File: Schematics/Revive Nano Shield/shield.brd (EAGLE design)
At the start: 35.6 x 63.5 mm, 24 parts

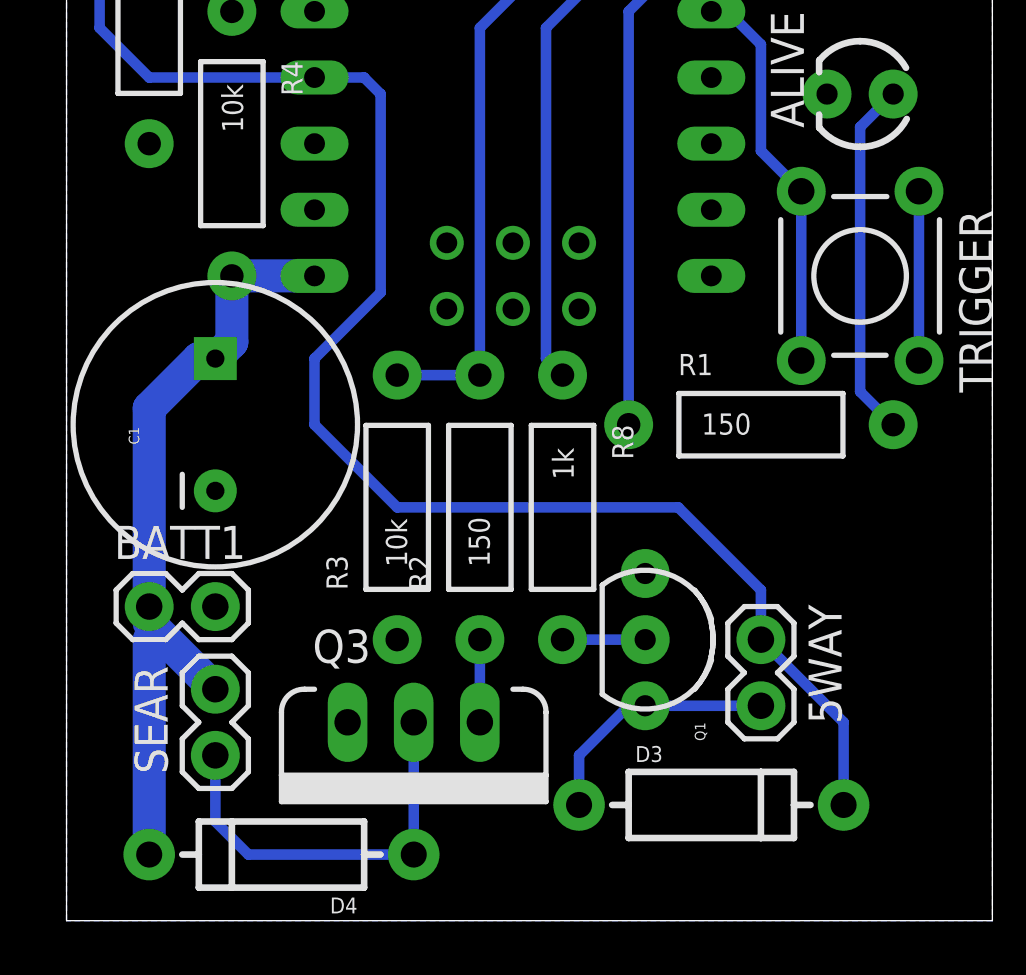
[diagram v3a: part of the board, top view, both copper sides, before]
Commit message: Moved around connectors to make them more accessible
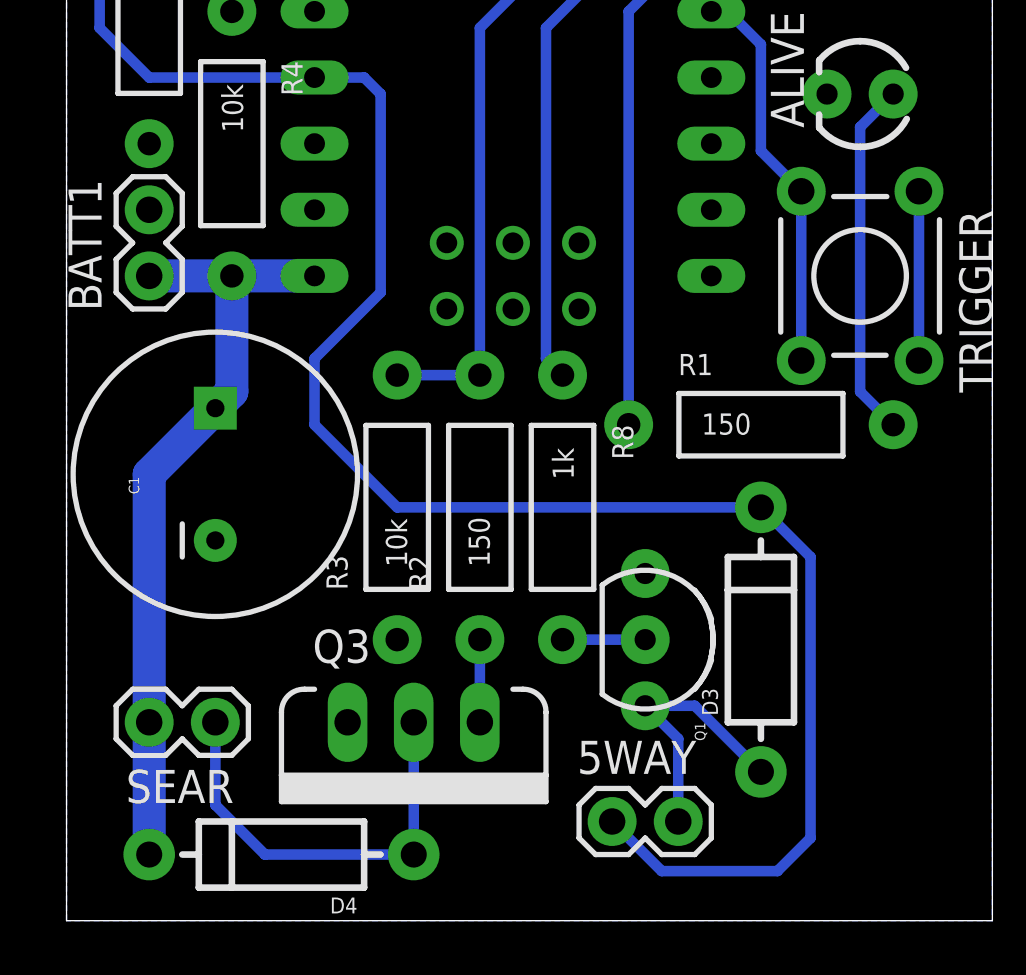
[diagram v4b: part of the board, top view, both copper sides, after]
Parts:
- moved BATT1 12.7 mm to (3.17, 24.8), turned to 90 degrees
- moved 5WAY 9.03 mm to (21.0, 3.81), turned to 0 degrees
- moved D3 6.63 mm to (26.7, 10.8), turned to 90 degrees
- moved SEAR 2.84 mm to (3.17, 7.62), turned to 0 degrees
- moved C1 1.91 mm to (5.71, 17.1)
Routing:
- net 5V: track 72.0 -> 83.5 mm
- net 9V: track 31.3 -> 29.9 mm
- net N$7: track 15.8 -> 16.7 mm
- net N$15: track 9.68 -> 10.5 mm
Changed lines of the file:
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@@
 </autorouter>
 <elements>
-<element name="5WAY" library="SparkFun" package="1X02" value="" x="26.67" y="10.795" rot="R270"/>
+<element name="5WAY" library="SparkFun" package="1X02" value="" x="20.955" y="3.81"/>
 <element name="ALIVE" library="SparkFun" package="LED3MM" value="" x="30.48" y="31.75" smashed="yes" rot="R180">
 <attribute name="NAME" x="27.051" y="34.925" size="1.27" layer="25" ratio="10" rot="R270"/>
 <attribute name="VALUE" x="28.575" y="33.401" size="1.27" layer="27" ratio="10" rot="R180"/>
 </element>
-<element name="BATT1" library="SparkFun" package="1X02" value="" x="3.175" y="12.065"/>
-<element name="C1" library="SparkFun" package="CPOL-RADIAL-1000UF-25V" value="2200uF" x="5.715" y="19.05" rot="R90"/>
-<element name="D3" library="SparkFun" package="DIODE-1N4001" value="" x="24.765" y="4.445"/>
+<element name="BATT1" library="SparkFun" package="1X02" value="" x="3.175" y="24.765" rot="R90"/>
+<element name="C1" library="SparkFun" package="CPOL-RADIAL-1000UF-25V" value="2200uF" x="5.715" y="17.145" rot="R90"/>
+<element name="D3" library="SparkFun" package="DIODE-1N4001" value="" x="26.67" y="10.795" rot="R90"/>
 <element name="D4" library="SparkFun" package="DIODE-1N4001" value="" x="8.255" y="2.54" rot="R180"/>
 <element name="DOWN" library="SparkFun" package="TACTILE-PTH" value="" x="30.48" y="57.785" rot="R270"/>
@@
 <element name="R6" library="SparkFun" package="AXIAL-0.4" value="1M" x="6.35" y="43.18" rot="R90"/>
 <element name="R8" library="SparkFun" package="AXIAL-0.4" value="1k" x="19.05" y="15.875" rot="R270"/>
-<element name="SEAR" library="SparkFun" package="1X02" value="" x="5.715" y="8.89" smashed="yes" rot="R270">
-<attribute name="NAME" x="3.8862" y="5.6388" size="1.27" layer="25" ratio="10" rot="R90"/>
-<attribute name="VALUE" x="2.54" y="10.16" size="1.27" layer="27" rot="R270"/>
+<element name="SEAR" library="SparkFun" package="1X02" value="" x="3.175" y="7.62" smashed="yes">
+<attribute name="NAME" x="6.4262" y="5.7912" size="1.27" layer="25" ratio="10" rot="R180"/>
+<attribute name="VALUE" x="1.905" y="4.445" size="1.27" layer="27"/>
 </element>
 <element name="SEL" library="SparkFun" package="TACTILE-PTH" value="" x="30.48" y="48.895" rot="R270"/>
@@
 <contactref element="C1" pad="1"/>
 <contactref element="R4" pad="P$2"/>
-<wire x1="3.175" y1="12.065" x2="3.175" y2="11.43" width="0.4064" layer="16"/>
-<wire x1="3.175" y1="11.43" x2="3.175" y2="10.795" width="0.4064" layer="16"/>
-<wire x1="3.175" y1="10.795" x2="3.81" y2="10.795" width="0.4064" layer="16"/>
 <wire x1="9.525" y1="24.765" x2="6.35" y2="24.765" width="1.27" layer="16"/>
-<wire x1="6.35" y1="24.765" x2="6.35" y2="22.225" width="1.27" layer="16"/>
-<wire x1="6.35" y1="22.225" x2="5.715" y2="21.59" width="1.27" layer="16"/>
-<wire x1="5.715" y1="21.59" x2="5.08" y2="21.59" width="1.27" layer="16"/>
-<wire x1="5.08" y1="21.59" x2="3.175" y2="19.685" width="1.27" layer="16"/>
-<wire x1="3.175" y1="19.685" x2="3.175" y2="12.065" width="1.27" layer="16"/>
-<wire x1="3.175" y1="10.795" x2="3.175" y2="2.54" width="1.27" layer="16"/>
-<wire x1="5.715" y1="8.89" x2="3.175" y2="11.43" width="1.27" layer="16"/>
+<wire x1="3.175" y1="24.765" x2="6.35" y2="24.765" width="1.27" layer="16"/>
+<wire x1="6.35" y1="24.765" x2="6.35" y2="20.32" width="1.27" layer="16"/>
+<wire x1="6.35" y1="20.32" x2="5.715" y2="19.685" width="1.27" layer="16"/>
+<wire x1="5.715" y1="19.685" x2="3.175" y2="17.145" width="1.27" layer="16"/>
+<wire x1="3.175" y1="17.145" x2="3.175" y2="7.62" width="1.27" layer="16"/>
+<wire x1="3.175" y1="7.62" x2="3.175" y2="2.54" width="1.27" layer="16"/>
 </signal>
 <signal name="GND">
@@
 <contactref element="D3" pad="C"/>
 <contactref element="5WAY" pad="1"/>
-<wire x1="29.845" y1="4.445" x2="29.845" y2="7.62" width="0.4064" layer="16"/>
-<wire x1="29.845" y1="7.62" x2="26.67" y2="10.795" width="0.4064" layer="16"/>
-<wire x1="26.67" y1="10.795" x2="26.67" y2="12.7" width="0.4064" layer="16"/>
-<wire x1="26.67" y1="12.7" x2="23.495" y2="15.875" width="0.4064" layer="16"/>
-<wire x1="23.495" y1="15.875" x2="12.7" y2="15.875" width="0.4064" layer="16"/>
+<wire x1="26.67" y1="15.875" x2="12.7" y2="15.875" width="0.4064" layer="16"/>
+<wire x1="20.955" y1="3.81" x2="22.86" y2="1.905" width="0.4064" layer="16"/>
+<wire x1="22.86" y1="1.905" x2="27.305" y2="1.905" width="0.4064" layer="16"/>
+<wire x1="27.305" y1="1.905" x2="28.575" y2="3.175" width="0.4064" layer="16"/>
+<wire x1="28.575" y1="3.175" x2="28.575" y2="13.97" width="0.4064" layer="16"/>
+<wire x1="28.575" y1="13.97" x2="26.67" y2="15.875" width="0.4064" layer="16"/>
 </signal>
 <signal name="TRIGGER">
@@
 <contactref element="D3" pad="A"/>
 <contactref element="5WAY" pad="2"/>
-<wire x1="26.67" y1="8.255" x2="22.225" y2="8.255" width="0.4064" layer="16"/>
-<wire x1="22.225" y1="8.255" x2="21.59" y2="8.255" width="0.4064" layer="16"/>
-<wire x1="21.59" y1="8.255" x2="19.685" y2="6.35" width="0.4064" layer="16"/>
-<wire x1="19.685" y1="6.35" x2="19.685" y2="4.445" width="0.4064" layer="16"/>
+<wire x1="22.225" y1="8.255" x2="24.13" y2="8.255" width="0.4064" layer="16"/>
+<wire x1="24.13" y1="8.255" x2="26.67" y2="5.715" width="0.4064" layer="16"/>
+<wire x1="23.495" y1="3.81" x2="23.495" y2="6.985" width="0.4064" layer="16"/>
+<wire x1="23.495" y1="6.985" x2="22.225" y2="8.255" width="0.4064" layer="16"/>
 </signal>
 <signal name="UP_BTN">
@@
 <contactref element="Q3" pad="2"/>
 <contactref element="SEAR" pad="2"/>
-<wire x1="13.335" y1="2.54" x2="6.985" y2="2.54" width="0.4064" layer="16"/>
 <wire x1="13.335" y1="2.54" x2="13.335" y2="7.62" width="0.4064" layer="16"/>
-<wire x1="5.715" y1="6.35" x2="5.715" y2="3.81" width="0.4064" layer="16"/>
-<wire x1="5.715" y1="3.81" x2="6.985" y2="2.54" width="0.4064" layer="16"/>
+<wire x1="5.715" y1="7.62" x2="5.715" y2="4.445" width="0.4064" layer="16"/>
+<wire x1="5.715" y1="4.445" x2="7.62" y2="2.54" width="0.4064" layer="16"/>
+<wire x1="7.62" y1="2.54" x2="13.335" y2="2.54" width="0.4064" layer="16"/>
 </signal>
 <signal name="N$1">

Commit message: Updated schematics
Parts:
- removed SENSOR: (no value), SparkFun:1X04
- added A/C_EYE: (no value), SparkFun:1X04
- added SLG_EYE: (no value), SparkFun-Connectors:1X03
- added SPI: (no value), SparkFun-Connectors:1X07
- R4, R5, R6, R9: device SparkFun:AXIAL-0.4 -> resistor:0309V
- moved R6 20.4 mm to (4.45, 63.5), turned to 0 degrees
- moved R9 19.1 mm to (6.35, 36.8)
- moved R5 14.7 mm to (4.45, 49.5), turned to 0 degrees
- moved I2C 14.6 mm to (3.17, 46.4)
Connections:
- net SCL renamed I2C_CLK
- net SDA renamed I2C_SDA
- removed net IRED: SENSOR.2, U$5.A2
- removed net N$6: R5.P$1, SENSOR.1
- removed net SENSOR: R6.P$2, SENSOR.3, U$5.A0
- new net EYE_GND: A/C_EYE.1, R5.1
- new net EYE_PWR: A/C_EYE.2, SLG_EYE.2, U$5.A2
- new net EYE_READ: A/C_EYE.3, R6.2, SLG_EYE.1, U$5.A0
- new net N$12: U$5.TX0
- new net N$13: U$5.RX1
- new net SPI_CLK: SPI.3, U$5.D13
- new net SPI_CS: SPI.7, U$5.D9
- new net SPI_DC: SPI.6, U$5.D10
- new net SPI_MOSI: SPI.5, U$5.D11
- new net SPI_RES: SPI.4, U$5.D12
- net 5V: now also A/C_EYE.4, SPI.2; no longer SENSOR.4
- net 9V: now also R4.2; no longer R4.P$2
- net BATT_STATUS: now also R4.1, R9.2; no longer R4.P$1, R9.P$2
- net DWN_BTN: now also U$5.D8; no longer U$5.D12
- net GND: now also R5.2, R6.1, R9.1, SLG_EYE.3, SPI.1; no longer R5.P$2, R6.P$1, R9.P$1
- net OLED_PWR: now also U$5.A3; no longer U$5.D13
- net SEL_BTN: now also U$5.D7; no longer U$5.D11
- net UP_BTN: now also U$5.D6; no longer U$5.D10
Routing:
- net 5V: track 83.5 -> 135.7 mm
- net EYE_PWR: track 0.00 -> 37.6 mm
- net I2C_CLK: track 39.5 -> 6.88 mm
- net I2C_SDA: track 38.2 -> 6.88 mm
- net SPI_CLK: track 0.00 -> 27.1 mm
- net BATT_STATUS: track 45.5 -> 21.4 mm
- net EYE_READ: track 0.00 -> 18.9 mm
- net SPI_CS: track 0.00 -> 16.8 mm
- net SENSOR: track 15.0 -> 0.00 mm
- net UP_BTN: track 25.6 -> 10.7 mm
- net SPI_DC: track 0.00 -> 12.9 mm
- net SPI_MOSI: track 0.00 -> 9.42 mm
- net IRED: track 7.40 -> 0.00 mm
- net 9V: track 29.9 -> 37.3 mm
- net SPI_RES: track 0.00 -> 5.61 mm
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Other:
- board size 35.6 x 63.5 mm -> 35.6 x 69.8 mm

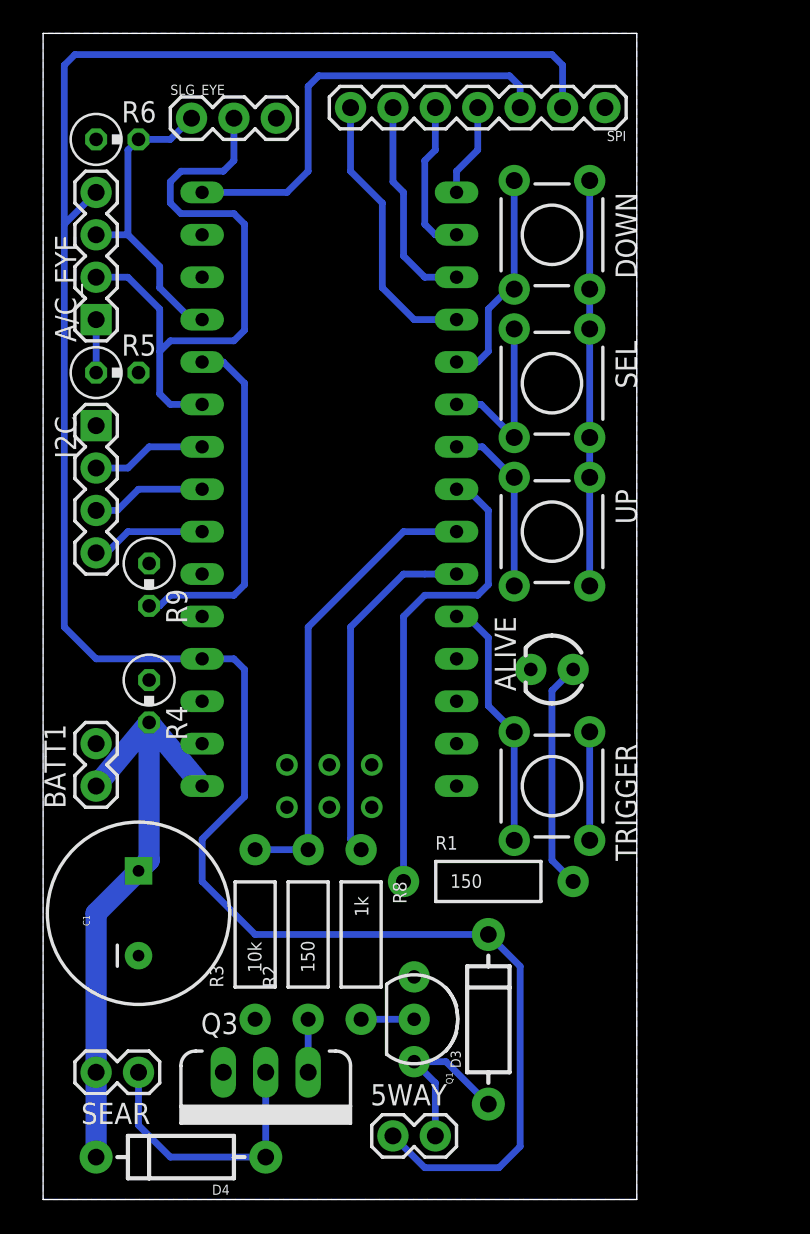
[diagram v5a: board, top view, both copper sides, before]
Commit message: Tweaked board layout to fit everything nicer
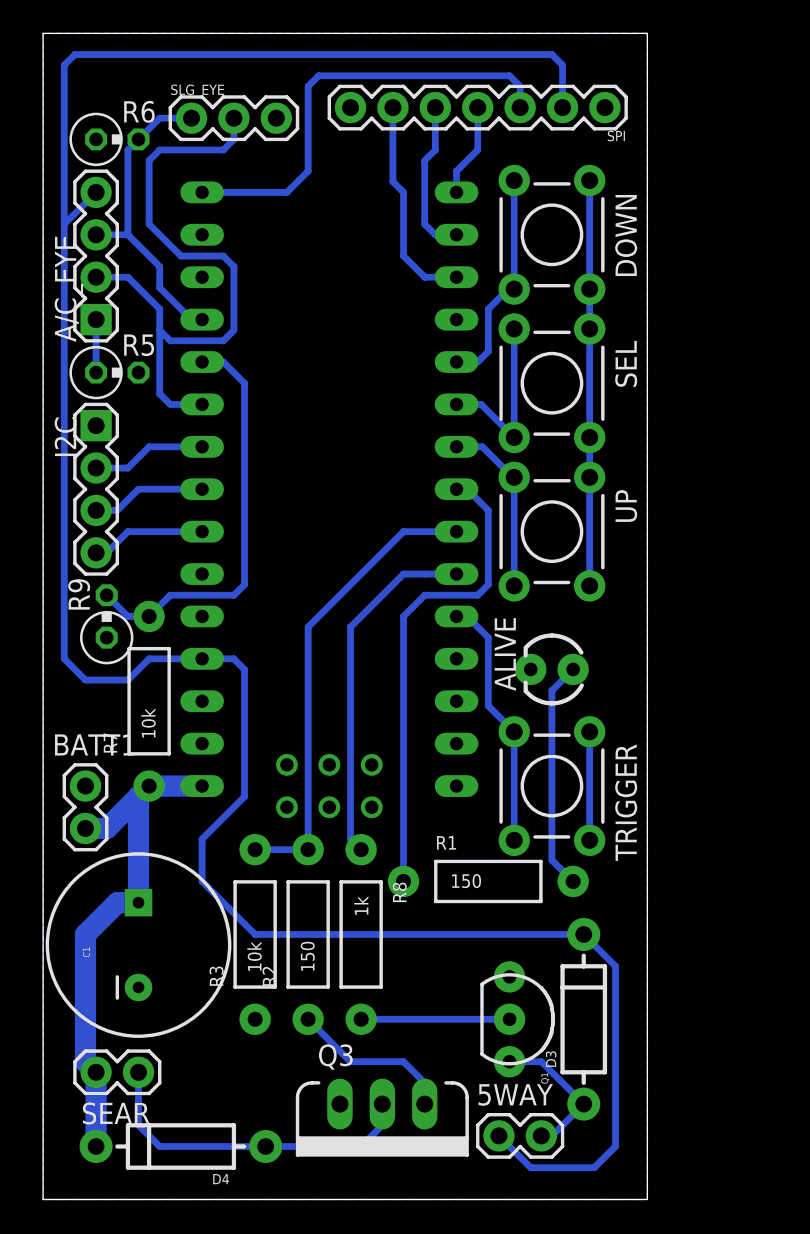
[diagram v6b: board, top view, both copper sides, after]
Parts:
- removed R4: 10k, resistor:0309V
- added R7: 10k, SparkFun:AXIAL-0.4
- moved Q3 7.24 mm to (20.3, 5.71)
- moved 5WAY 6.35 mm to (27.3, 3.81)
- moved Q1 5.71 mm to (27.9, 10.8)
- moved D3 5.71 mm to (32.4, 10.8)
- moved R9 3.18 mm to (3.81, 34.9), turned to 90 degrees
- moved BATT1 2.62 mm to (2.54, 22.2)
- moved C1 1.90 mm to (5.71, 15.2)
- moved D4 0.63 mm to (8.26, 3.17)
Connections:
- removed net SPI_CS: SPI.7, U$5.D9
- net 9V: now also R7.P$1; no longer R4.2
- net BATT_STATUS: now also R7.P$2; no longer R4.1
- net GND: now also SPI.7
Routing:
- net SPI_CS: track 16.8 -> 0.00 mm
- net 5V: track 135.7 -> 143.0 mm
- net N$3: track 3.17 -> 9.83 mm
- net N$1: track 3.18 -> 8.89 mm
- net 9V: track 37.3 -> 32.2 mm
- net N$7: track 16.7 -> 20.1 mm
- net BATT_STATUS: track 21.4 -> 24.7 mm
- net N$15: track 10.5 -> 8.83 mm
- net EYE_PWR: track 37.6 -> 38.1 mm
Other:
- board size 35.6 x 69.8 mm -> 36.2 x 69.8 mm
